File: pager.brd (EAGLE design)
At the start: 78.4 x 44.8 mm, 62 parts, among them Q1 25 MHz, Q2 SI2333DS, SW1 CHS-01A1, SW2 CHS-01A1, U1 VOCORE2-SMD, U2 VOCORE2-SMD, U3 XR22800IL, X1 OMRON_XF2L-30REVERSE, X2 FCI_8193_MICRO_USB

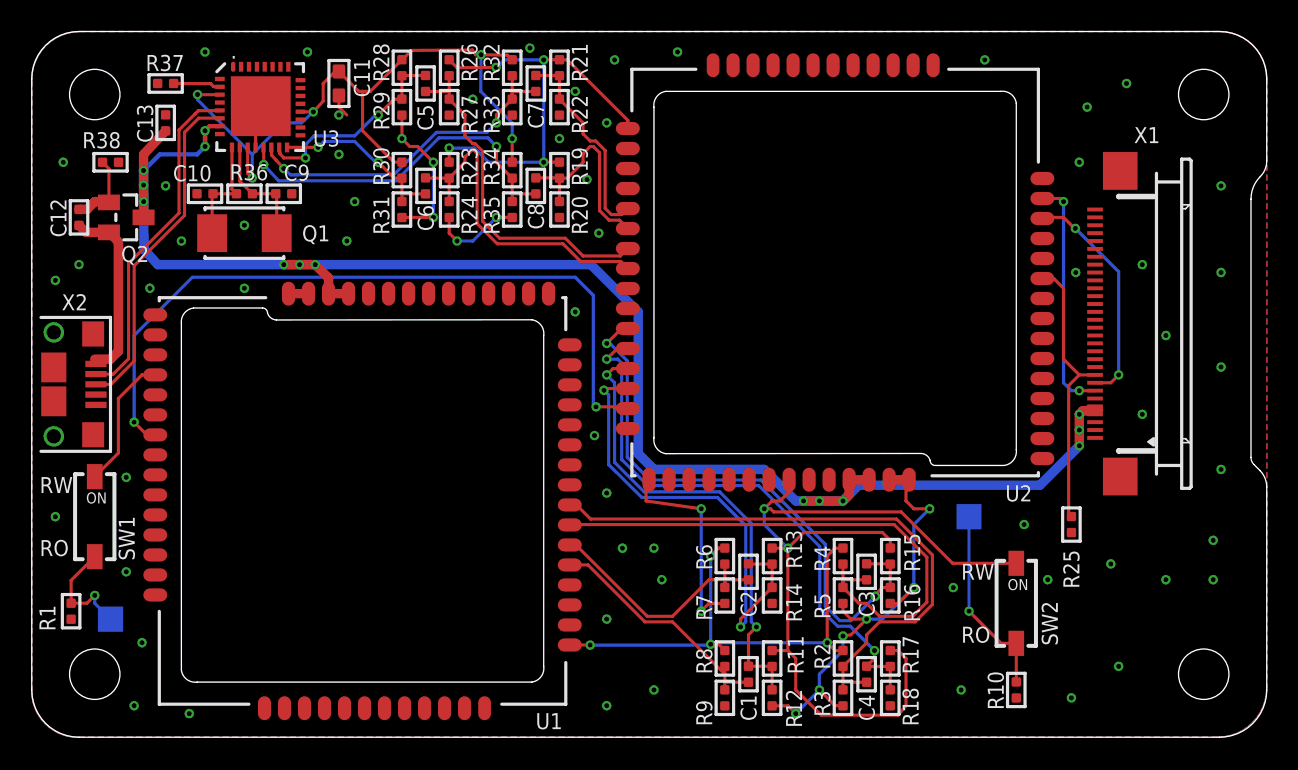
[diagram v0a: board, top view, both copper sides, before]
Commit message: Ground planes even nicer
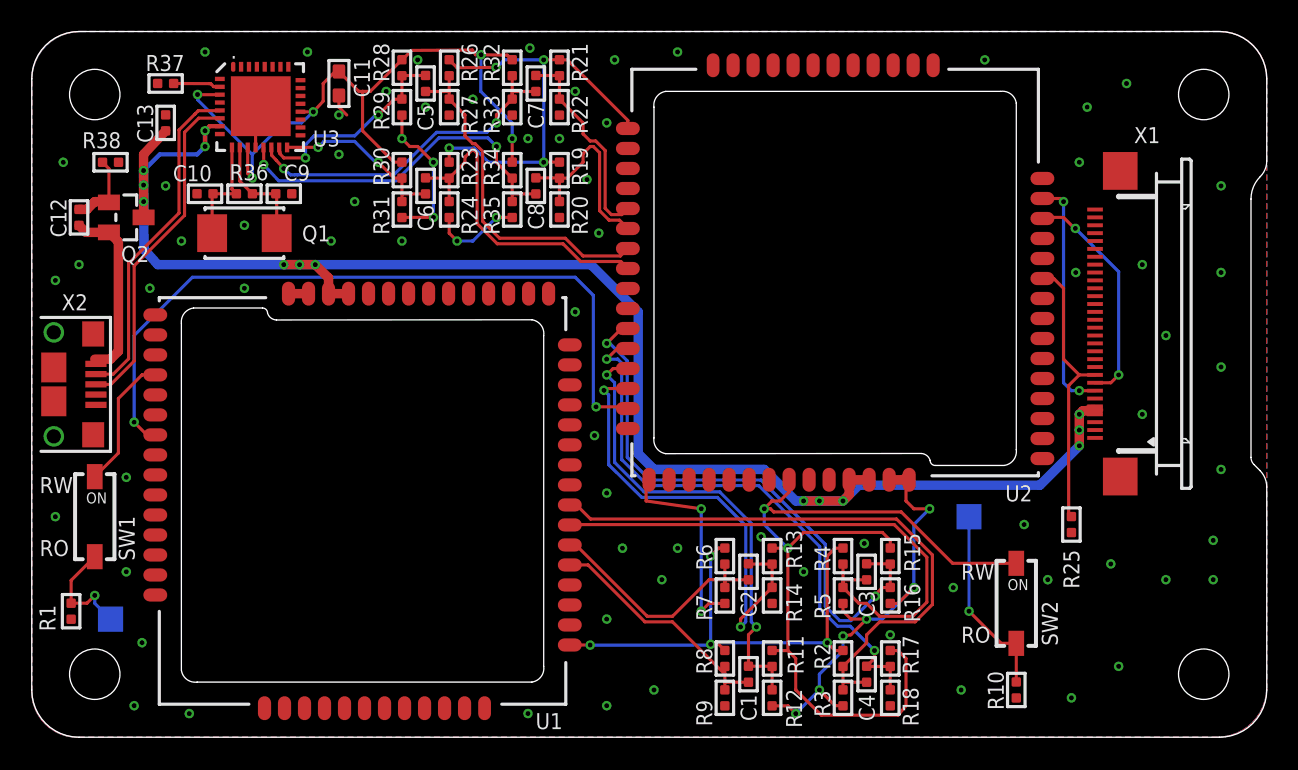
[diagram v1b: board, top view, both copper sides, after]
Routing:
- net GND: vias 73 -> 83
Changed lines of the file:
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@@
 <wire x1="52" y1="6.5" x2="53" y2="7.5" width="0.2" layer="1"/>
 <via x="67" y="40" extent="1-16" drill="0.3048"/>
-<via x="39.5" y="12" extent="1-16" drill="0.3048"/>
+<via x="41" y="12" extent="1-16" drill="0.3048"/>
 <via x="69" y="4.5" extent="1-16" drill="0.3048"/>
 <via x="8.5" y="35" extent="1-16" drill="0.3048"/>
@@
 <via x="6.5" y="2" extent="1-16" drill="0.3048"/>
 <via x="10" y="1.5" extent="1-16" drill="0.3048"/>
-<via x="20" y="31.5" extent="1-16" drill="0.3048"/>
+<via x="19" y="31.5" extent="1-16" drill="0.3048"/>
 <via x="20.5" y="34" extent="1-16" drill="0.3048"/>
 <via x="37" y="43" extent="1-16" drill="0.3048"/>
@@
 <via x="28" y="40.5" extent="1-16" drill="0.3048"/>
 <via x="31.625" y="43.75" extent="1-16" drill="0.3048"/>
-<wire x1="47" y1="8.492" x2="44" y2="8.492" width="0" layer="19" extent="1-1"/>
+<via x="23.5" y="31.5" extent="1-16" drill="0.3048"/>
+<via x="49" y="10.5" extent="1-16" drill="0.3048"/>
+<via x="46.3" y="12.725" extent="1-16" drill="0.3048"/>
+<via x="54.5" y="6.5" extent="1-16" drill="0.3048"/>
+<via x="31.5" y="1.5" extent="1-16" drill="0.3048"/>
+<via x="25" y="40" extent="1-16" drill="0.3048"/>
+<via x="31.5" y="38" extent="1-16" drill="0.3048"/>
+<via x="22.5" y="41" extent="1-16" drill="0.3048"/>
+<via x="24.5" y="43" extent="1-16" drill="0.3048"/>
+<via x="52.85" y="12.3" extent="1-16" drill="0.3048"/>
+<wire x1="47" y1="8.492" x2="49" y2="10.5" width="0" layer="19" extent="1-1"/>
 </signal>
 <signal name="ETH_1B_TX_P" class="1">

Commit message: Added TVS, resistor and cap between USB-shield and GND, made +5V bus 0.8 mm thick
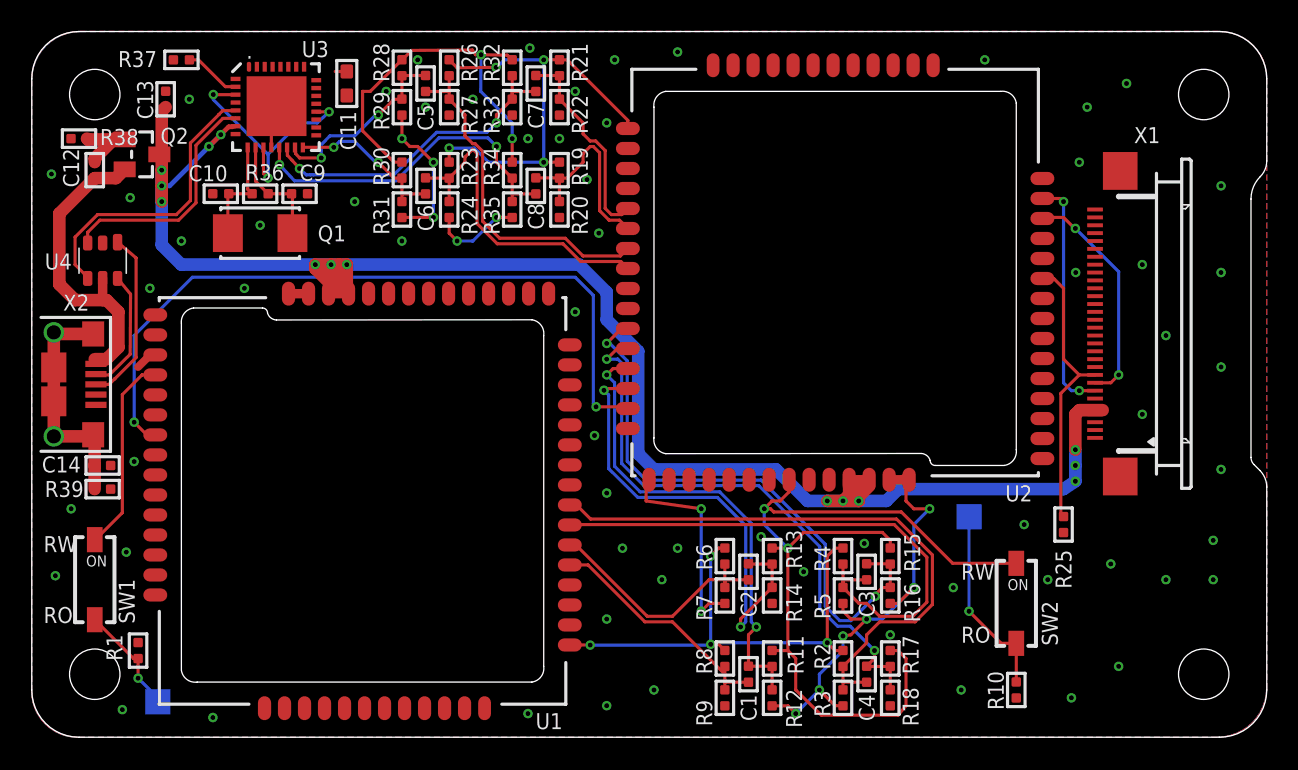
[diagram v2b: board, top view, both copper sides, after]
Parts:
- added C14: 100 nF, pager:_0402
- added R39: 1M, pager:_0402
- added U4: IP4234CZ6, pager:TSOP-6
- moved TP1 6.05 mm to (8.00, 2.25)
- moved R1 4.93 mm to (6.75, 5.50), turned to 270 degrees
- moved Q2 4.12 mm to (7.00, 37.0)
- moved SW1 4.00 mm to (4.00, 10.0)
- moved C12 3.16 mm to (4.00, 36.0)
- moved R38 2.50 mm to (3.00, 38.0), turned to 0 degrees
- moved R37 1.80 mm to (9.50, 43.0)
- moved C13 1.50 mm to (8.50, 40.5)
- moved C10 1.00 mm to (12.0, 34.5)
- moved C9 1.00 mm to (17.0, 34.5)
- moved Q1 1.00 mm to (14.5, 32.0)
- moved R36 1.00 mm to (14.5, 34.5)
- moved U3 1.00 mm to (15.5, 40.0)
- moved C11 0.50 mm to (20.0, 41.5)
- moved R25 0.50 mm to (65.5, 13.5)
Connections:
- removed net N$27: C12.1, Q2.2, X2.VBUS
- removed net USB_D_N: U3.28, X2.D-
- removed net USB_D_P: U3.27, X2.D+
- new net RAW_+5V: C12.1, Q2.2, U4.5, X2.VBUS
- new net SHIELD: C14.1, R39.2, X2.MNT1, X2.MNT2, X2.MNT3, X2.MNT4, X2.P$1, X2.P$2
- new net USB_N: U3.28, U4.4
- new net USB_P: U3.27, U4.3
- new net USB_RAW_N: U4.6, X2.D-
- new net USB_RAW_P: U4.1, X2.D+
- net GND: now also C14.2, R39.1, U4.2
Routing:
- net USB_D_P: track 21.5 -> 0.00 mm
- net USB_D_N: track 21.4 -> 0.00 mm
- net RAW_+5V: track 0.00 -> 20.0 mm
- net USB_N: track 0.00 -> 18.6 mm
- net USB_P: track 0.00 -> 15.2 mm
- net SHIELD: track 0.00 -> 15.1 mm
- net N$27: track 12.0 -> 0.00 mm
- net USB_RAW_P: track 0.00 -> 11.1 mm
- net USB_RAW_N: track 0.00 -> 7.84 mm
- net +5V: track 106.6 -> 112.9 mm
- net 3.3_USB: track 45.7 -> 41.1 mm
- net 3.3_WIFI: track 40.7 -> 44.7 mm
- net GND: track 63.4 -> 62.0 mm, vias 83 -> 77
- net N$2: track 0.00 -> 1.06 mm
- net ETH_1B_TX_P: track 22.1 -> 21.1 mm
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
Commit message: minor fixes
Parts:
- moved C14 0.25 mm to (4.50, 17.0)
- moved R39 0.25 mm to (4.50, 15.5)
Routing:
- net GND: track 62.0 -> 63.0 mm, vias 77 -> 78
- net N$2: track 1.06 -> 0.00 mm
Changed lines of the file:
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@@
 <attribute name="VALUE" x="-1.6" y="26.4" size="1.27" layer="27" font="vector" rot="R270"/>
 </element>
-<element name="C14" library="pager" package="_0402" value="100 nF" x="4.5" y="17.25" smashed="yes">
-<attribute name="NAME" x="0.6425" y="16.8064" size="1.016" layer="25" font="vector" ratio="14"/>
-<attribute name="VALUE" x="3.23" y="15.9164" size="0.508" layer="27" font="vector" ratio="10"/>
+<element name="C14" library="pager" package="_0402" value="100 nF" x="4.5" y="17" smashed="yes">
+<attribute name="NAME" x="0.6425" y="16.5564" size="1.016" layer="25" font="vector" ratio="14"/>
+<attribute name="VALUE" x="3.23" y="15.6664" size="0.508" layer="27" font="vector" ratio="10"/>
 </element>
-<element name="R39" library="pager" package="_0402" value="1M" x="4.5" y="15.75" smashed="yes" rot="R180">
-<attribute name="NAME" x="3.295" y="16.2686" size="1.016" layer="25" font="vector" ratio="14" rot="R180"/>
-<attribute name="VALUE" x="5.77" y="17.0836" size="0.508" layer="27" font="vector" ratio="10" rot="R180"/>
+<element name="R39" library="pager" package="_0402" value="1M" x="4.5" y="15.5" smashed="yes" rot="R180">
+<attribute name="NAME" x="3.295" y="16.0186" size="1.016" layer="25" font="vector" ratio="14" rot="R180"/>
+<attribute name="VALUE" x="5.77" y="16.8336" size="0.508" layer="27" font="vector" ratio="10" rot="R180"/>
 </element>
 </elements>
@@
 <via x="10" y="40.5" extent="1-16" drill="0.3048"/>
 <via x="6.25" y="34.25" extent="1-16" drill="0.3048"/>
+<wire x1="7.5" y1="24.25" x2="6.75" y2="23.5" width="0.5" layer="1"/>
 <wire x1="47" y1="8.492" x2="49" y2="10.5" width="0" layer="19" extent="1-1"/>
+<via x="2.75" y="22.5" extent="1-16" drill="0.3048"/>
 </signal>
 <signal name="ETH_1B_TX_P" class="1">
@@
 <wire x1="1.4" y1="19.1" x2="3.8" y2="19.1" width="0.8" layer="1"/>
 <wire x1="3.8" y1="19.1" x2="3.9" y2="19.2" width="0.8" layer="1"/>
-<wire x1="3.992" y1="15.75" x2="3.992" y2="17.25" width="0.8" layer="1"/>
+<wire x1="3.992" y1="15.5" x2="3.992" y2="17" width="0.8" layer="1"/>
 <wire x1="3.8" y1="19.1" x2="3.992" y2="18.908" width="0.8" layer="1"/>
-<wire x1="3.992" y1="18.908" x2="3.992" y2="17.25" width="0.8" layer="1"/>
+<wire x1="3.992" y1="18.908" x2="3.992" y2="17" width="0.8" layer="1"/>
 </signal>
 <signal name="USB_N" class="2">
@@
 <wire x1="12.93790625" y1="39.28790625" x2="12.94" y2="39.29" width="0.2" layer="1"/>
 </signal>
-<signal name="N$2">
-<wire x1="7.5" y1="24.25" x2="6.75" y2="23.5" width="0.5" layer="1"/>
-</signal>
 </signals>

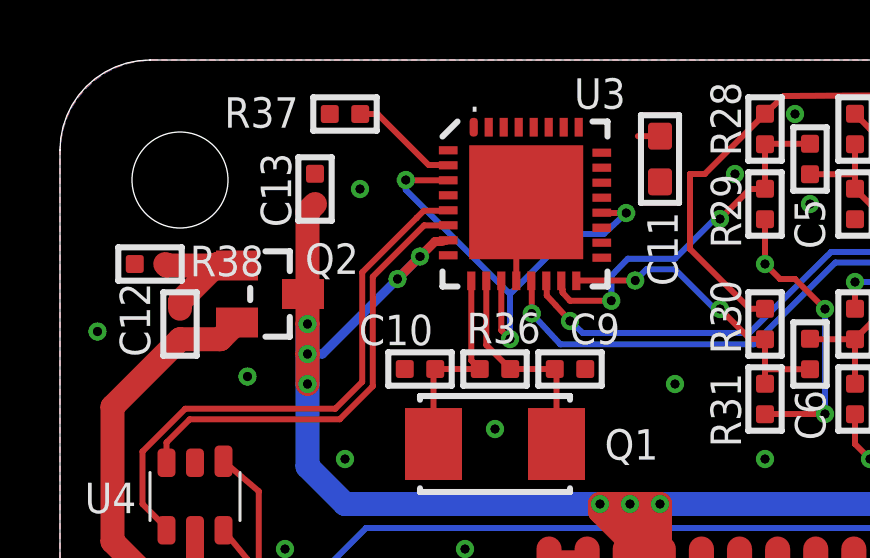
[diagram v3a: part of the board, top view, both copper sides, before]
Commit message: two more GND vias
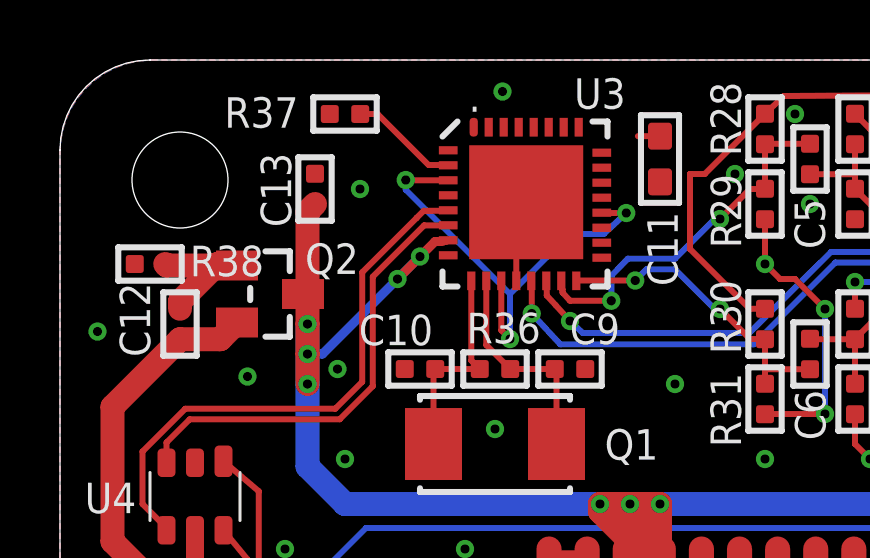
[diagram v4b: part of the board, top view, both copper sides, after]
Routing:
- net GND: vias 78 -> 80
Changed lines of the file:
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@@
 <wire x1="47" y1="8.492" x2="49" y2="10.5" width="0" layer="19" extent="1-1"/>
 <via x="2.75" y="22.5" extent="1-16" drill="0.3048"/>
+<via x="9.25" y="34.5" extent="1-16" drill="0.3048"/>
+<via x="14.75" y="43.75" extent="1-16" drill="0.3048"/>
 </signal>
 <signal name="ETH_1B_TX_P" class="1">

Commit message: various small fixes
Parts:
- moved R38 2.06 mm to (2.50, 36.0), turned to 90 degrees
- moved R1 1.58 mm to (6.25, 7.00)
- moved SW1 0.50 mm to (3.50, 10.0)
- moved TP2 0.50 mm to (59.5, 13.5)
- moved U4 0.25 mm to (4.50, 30.0)
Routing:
- net GND: track 63.0 -> 68.8 mm, vias 80 -> 84
- net WP_WIFI: track 7.03 -> 8.20 mm
- net N$28: track 5.09 -> 4.18 mm
- net USB_N: track 18.6 -> 19.2 mm
- net WP_CORE: track 12.3 -> 11.8 mm
- net 3.3_WIFI: track 44.7 -> 45.2 mm
- net +5V: track 112.9 -> 113.4 mm

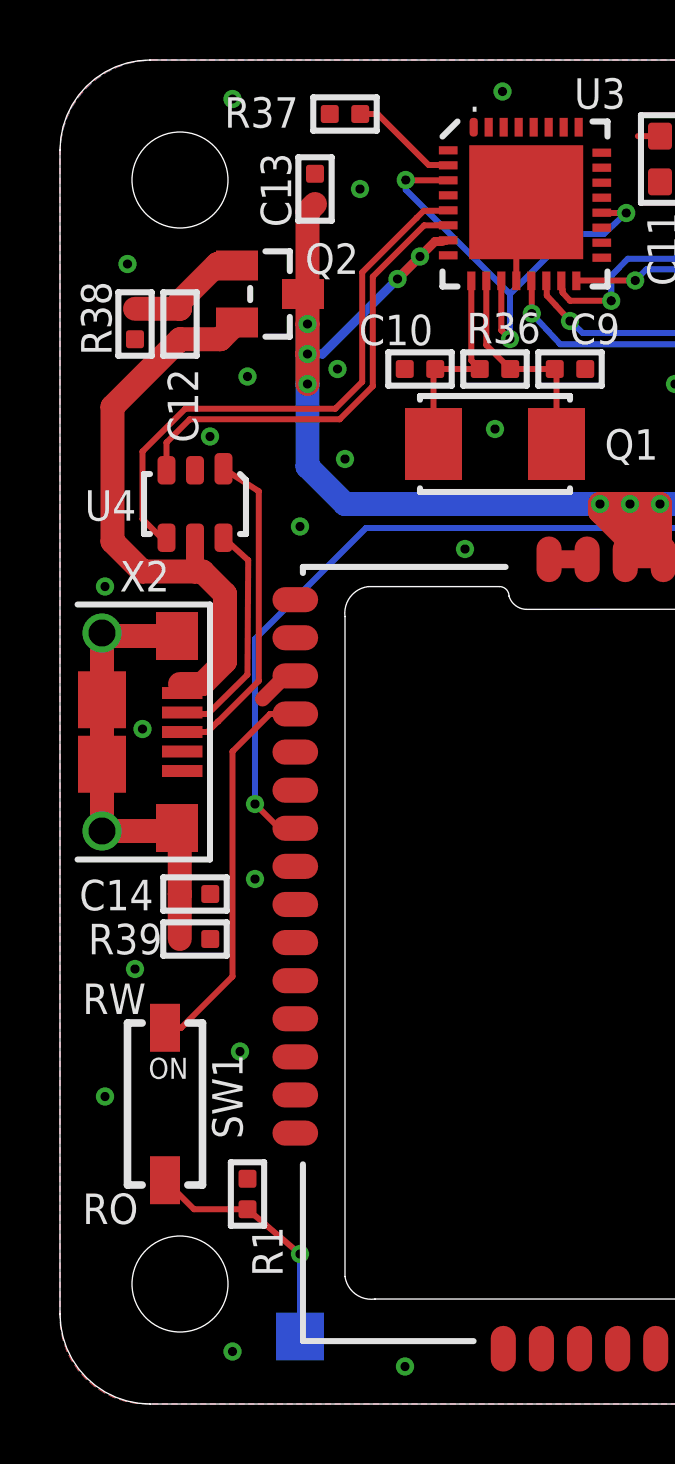
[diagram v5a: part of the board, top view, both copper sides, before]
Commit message: moves to make more space around mounting holes
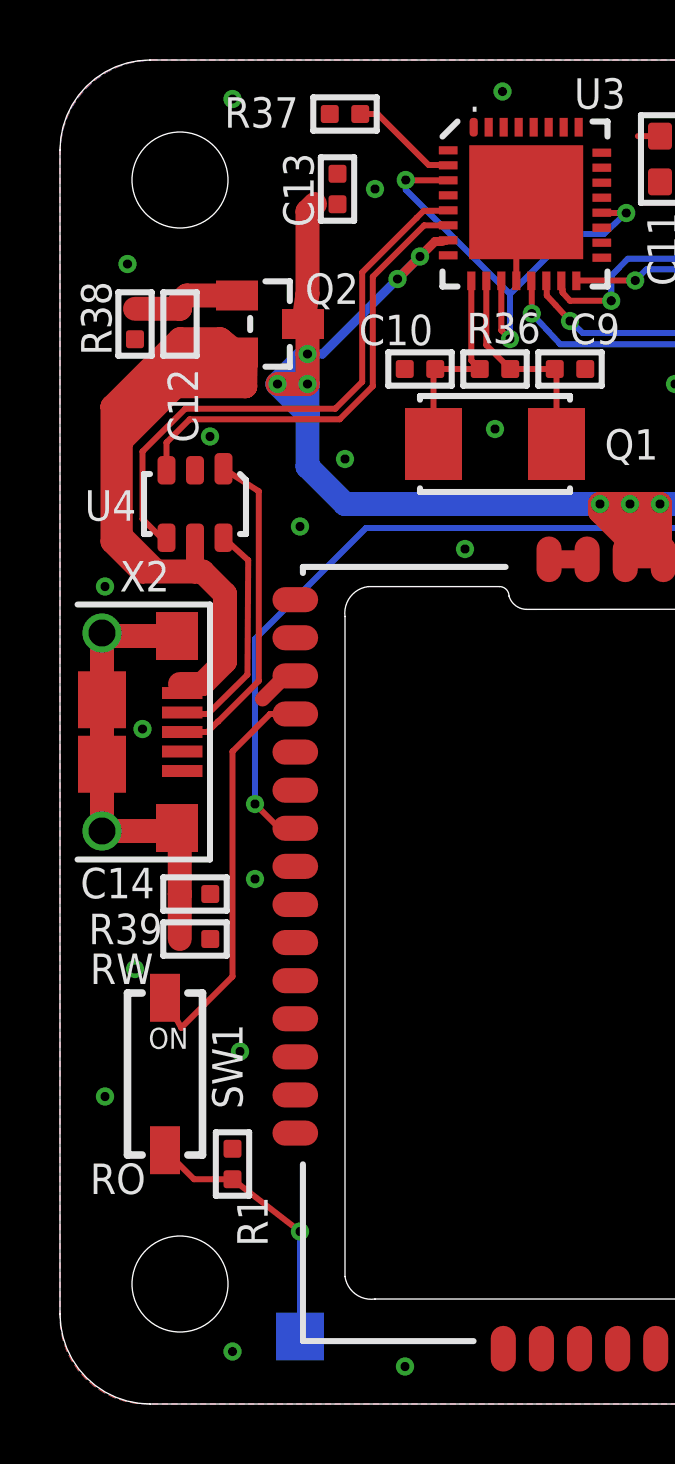
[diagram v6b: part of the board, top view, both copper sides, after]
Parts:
- moved R1 1.12 mm to (5.75, 8.00)
- moved Q2 1.00 mm to (7.00, 36.0)
- moved SW1 1.00 mm to (3.50, 11.0)
- moved C13 0.75 mm to (9.25, 40.5)
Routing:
- net RAW_+5V: track 19.8 -> 41.2 mm
- net +5V: track 113.4 -> 117.1 mm
- net WP_WIFI: track 8.20 -> 9.00 mm
- net 3.3_WIFI: track 45.2 -> 45.8 mm
- net GND: vias 84 -> 82
